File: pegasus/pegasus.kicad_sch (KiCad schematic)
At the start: 16 parts, among them IC1 L7805ACV, IC2 RFD900, IC3 L70B-M39, J1 Screw_Terminal_01x02, U1 Teensy4.0, U2 CON-SMA-EDGE-S, U3 CON-SMA-EDGE-S

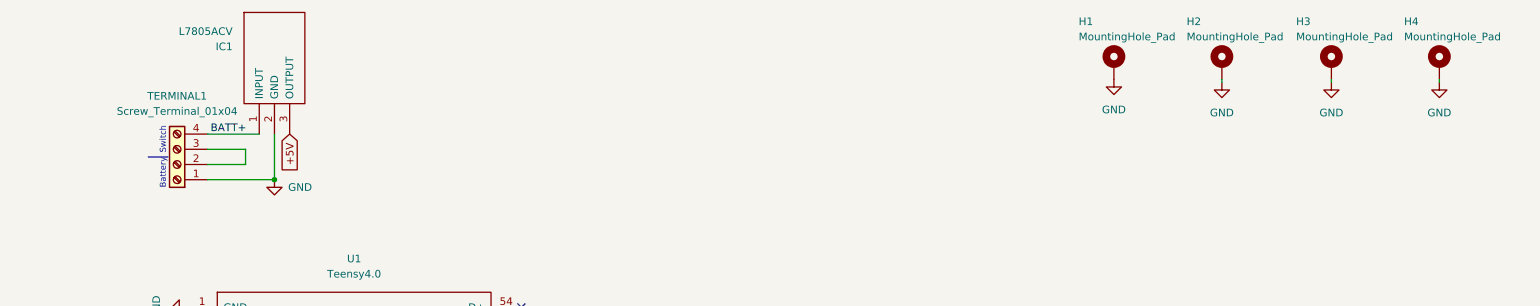
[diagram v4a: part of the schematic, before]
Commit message: change mount holes to m3, draft new component layout, reduce size  to 39x105mm
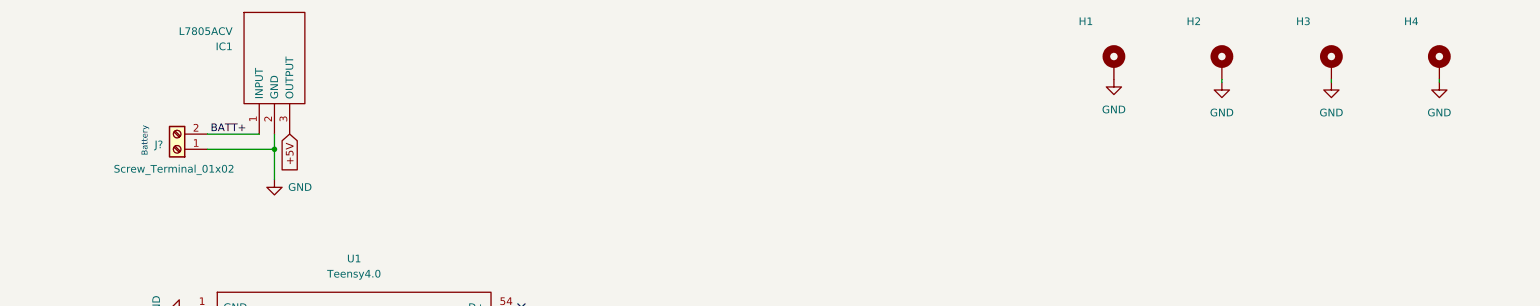
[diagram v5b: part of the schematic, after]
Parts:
- removed TERMINAL1: Screw_Terminal_01x04, RS-Components:SHDR4W100P0X500_1X4_2000X800X1000P, symbol Connector:Screw_Terminal_01x04
- added J?: Screw_Terminal_01x02, RS-Components:SHDR2W105P0X500_1X2_1060X900X1250P, symbol Connector:Screw_Terminal_01x02
- H1, H2, H3, H4: value MountingHole_Pad -> (none); footprint MountingHole:MountingHole_2.2mm_M2_Pad -> (none)
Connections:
- net BATT+: now also J?.2 (Pin_2)
- net GND: now also J?.1 (Pin_1)
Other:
- note removed: "Switch"
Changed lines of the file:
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@@
     (rev "1")
   )
-  (junction (at 56.134 42.164) (diameter 0) (color 0 0 0 0)
+  (junction (at 56.134 37.084) (diameter 0) (color 0 0 0 0)
   )
   (no_connect (at 97.3836 91.44))
@@
     (stroke (width 0) (type default) (color 0 0 0 0))
   )
-  (wire (pts (xy 56.134 34.544) (xy 56.134 42.164))
+  (wire (pts (xy 56.134 34.544) (xy 56.134 37.084))
     (stroke (width 0) (type default) (color 0 0 0 0))
   )
@@
     (stroke (width 0) (type default) (color 0 0 0 0))
   )
-  (wire (pts (xy 51.308 39.624) (xy 51.308 37.084))
-    (stroke (width 0) (type default) (color 0 0 0 0))
-  )
-  (wire (pts (xy 44.958 42.164) (xy 56.134 42.164))
-    (stroke (width 0) (type default) (color 0 0 0 0))
-  )
-  (wire (pts (xy 51.308 39.624) (xy 44.958 39.624))
+  (wire (pts (xy 44.958 37.084) (xy 56.134 37.084))
     (stroke (width 0) (type default) (color 0 0 0 0))
   )
@@
     (stroke (width 0) (type default) (color 0 0 0 0))
   )
-  (wire (pts (xy 51.308 37.084) (xy 44.958 37.084))
-    (stroke (width 0) (type default) (color 0 0 0 0))
-  )
-  (polyline (pts (xy 35.052 38.354) (xy 38.354 38.354))
-    (stroke (width 0) (type default) (color 0 0 0 0))
-  )
   (polyline (pts (xy 55.0164 197.9168) (xy 54.8132 154.6352))
     (stroke (width 0) (type default) (color 0 0 0 0))
   )
   (wire (pts (xy 117.6528 188.595) (xy 119.2784 188.595))
+    (stroke (width 0) (type default) (color 0 0 0 0))
+  )
+  (wire (pts (xy 56.134 37.084) (xy 56.134 42.164))
     (stroke (width 0) (type default) (color 0 0 0 0))
   )
@@
     (effects (font (size 1.27 1.27)) (justify left bottom))
   )
-  (text "Switch\n" (at 38.1 37.846 90)
-    (effects (font (size 1 1)) (justify left bottom))
-  )
   (text "RGB LED" (at 29.0068 154.7876 0)
     (effects (font (size 3 3)) (justify left bottom))
   )
-  (text "Battery" (at 38.1 38.608 270)
+  (text "Battery" (at 35.052 33.274 270)
     (effects (font (size 1 1)) (justify right bottom))
   )
@@
     (pin "1")
   )
+  (symbol (lib_id "Connector:Screw_Terminal_01x02") (at 39.878 37.084 180) (unit 1)
+    (in_bom yes) (on_board yes)
+    (property "Reference" "J?" (id 0) (at 36.83 36.322 0))
+    (property "Value" "Screw_Terminal_01x02" (id 1) (at 39.37 40.386 0))
+    (property "Footprint" "RS-Components:SHDR2W105P0X500_1X2_1060X900X1250P" (id 2) (at 39.878 37.084 0)
+      (effects (font (size 1.27 1.27)) hide)
+    )
+    (property "Datasheet" "~" (id 3) (at 39.878 37.084 0)
+      (effects (font (size 1.27 1.27)) hide)
+    )
+    (pin "1")
+    (pin "2")
+  )
   (symbol (lib_id "power:GND") (at 145.9484 179.07 90) (unit 1)
     (in_bom yes) (on_board yes) (fields_autoplaced)
@@
       (effects (font (size 1.27 1.27)) (justify left))
     )
-    (property "Value" "MountingHole_Pad" (id 1) (at 244.8052 18.288 0)
-      (effects (font (size 1.27 1.27)) (justify left))
-    )
-    (property "Footprint" "MountingHole:MountingHole_2.2mm_M2_Pad" (id 2) (at 250.698 22.86 0)
+    (property "Value" "" (id 1) (at 244.8052 18.288 0)
+      (effects (font (size 1.27 1.27)) (justify left))
+    )
+    (property "Footprint" "" (id 2) (at 250.698 22.86 0)
       (effects (font (size 1.27 1.27)) hide)
     )
@@
       (effects (font (size 1.27 1.27)) (justify left))
     )
-    (property "Value" "MountingHole_Pad" (id 1) (at 208.4832 18.288 0)
-      (effects (font (size 1.27 1.27)) (justify left))
-    )
-    (property "Footprint" "MountingHole:MountingHole_2.2mm_M2_Pad" (id 2) (at 214.376 22.86 0)
+    (property "Value" "" (id 1) (at 208.4832 18.288 0)
+      (effects (font (size 1.27 1.27)) (justify left))
+    )
+    (property "Footprint" "" (id 2) (at 214.376 22.86 0)
       (effects (font (size 1.27 1.27)) hide)
     )
@@
       (effects (font (size 1.27 1.27)) (justify left))
     )
-    (property "Value" "MountingHole_Pad" (id 1) (at 226.7712 18.288 0)
-      (effects (font (size 1.27 1.27)) (justify left))
-    )
-    (property "Footprint" "MountingHole:MountingHole_2.2mm_M2_Pad" (id 2) (at 232.664 22.86 0)
+    (property "Value" "" (id 1) (at 226.7712 18.288 0)
+      (effects (font (size 1.27 1.27)) (justify left))
+    )
+    (property "Footprint" "" (id 2) (at 232.664 22.86 0)
       (effects (font (size 1.27 1.27)) hide)
     )
@@
     )
     (pin "1")
-  )
-  (symbol (lib_id "Connector:Screw_Terminal_01x04") (at 39.878 39.624 180) (unit 1)
-    (in_bom no) (on_board yes) (fields_autoplaced)
-    (property "Reference" "TERMINAL1" (id 0) (at 39.878 28.194 0))
-    (property "Value" "Screw_Terminal_01x04" (id 1) (at 39.878 30.734 0))
-    (property "Footprint" "RS-Components:SHDR4W100P0X500_1X4_2000X800X1000P" (id 2) (at 39.878 39.624 0)
-      (effects (font (size 1.27 1.27)) hide)
-    )
-    (property "Datasheet" "~" (id 3) (at 39.878 39.624 0)
-      (effects (font (size 1.27 1.27)) hide)
-    )
-    (pin "1")
-    (pin "2")
-    (pin "3")
-    (pin "4")
   )
   (symbol (lib_id "Device:R_US") (at 42.7736 175.1584 180) (unit 1)
@@
       (effects (font (size 1.27 1.27)) (justify left))
     )
-    (property "Value" "MountingHole_Pad" (id 1) (at 190.4492 18.288 0)
-      (effects (font (size 1.27 1.27)) (justify left))
-    )
-    (property "Footprint" "MountingHole:MountingHole_2.2mm_M2_Pad" (id 2) (at 196.342 22.86 0)
+    (property "Value" "" (id 1) (at 190.4492 18.288 0)
+      (effects (font (size 1.27 1.27)) (justify left))
+    )
+    (property "Footprint" "" (id 2) (at 196.342 22.86 0)
       (effects (font (size 1.27 1.27)) hide)
     )
@@
     )
     (path "/fa097515-aa33-445e-a81c-63a2092f37d7"
-      (reference "H1") (unit 1) (value "MountingHole_Pad") (footprint "MountingHole:MountingHole_2.2mm_M2_Pad")
+      (reference "H1") (unit 1) (value "MountingHole_Pad") (footprint "MountingHole:MountingHole_3.2mm_M3_Pad")
     )
     (path "/9b4a3d5d-bec5-404f-9d07-6bbf9e73bbb6"
-      (reference "H2") (unit 1) (value "MountingHole_Pad") (footprint "MountingHole:MountingHole_2.2mm_M2_Pad")
+      (reference "H2") (unit 1) (value "MountingHole_Pad") (footprint "MountingHole:MountingHole_3.2mm_M3_Pad")
     )
     (path "/b9ff2bc9-2909-44de-b87f-01ae5ef3e5c6"
-      (reference "H3") (unit 1) (value "MountingHole_Pad") (footprint "MountingHole:MountingHole_2.2mm_M2_Pad")
+      (reference "H3") (unit 1) (value "MountingHole_Pad") (footprint "MountingHole:MountingHole_3.2mm_M3_Pad")
     )
     (path "/6d52c2cd-3d4d-4e9f-8991-6c4289d279ca"
-      (reference "H4") (unit 1) (value "MountingHole_Pad") (footprint "MountingHole:MountingHole_2.2mm_M2_Pad")
+      (reference "H4") (unit 1) (value "MountingHole_Pad") (footprint "MountingHole:MountingHole_3.2mm_M3_Pad")
     )
     (path "/57cb0745-7118-4f35-b7ad-15a440e8d2d7"
@@
       (reference "J1") (unit 1) (value "Screw_Terminal_01x02") (footprint "RS-Components:SHDR2W105P0X500_1X2_1060X900X1250P")
     )
+    (path "/4a35e1c8-7550-4a41-b483-1eb383f06ddc"
+      (reference "J?") (unit 1) (value "Screw_Terminal_01x02") (footprint "RS-Components:SHDR2W105P0X500_1X2_1060X900X1250P")
+    )
     (path "/40c73c82-ef5d-488c-b0d1-acd056d22f6f"
       (reference "R1") (unit 1) (value "220") (footprint "Resistor_SMD:R_1206_3216Metric_Pad1.30x1.75mm_HandSolder")
@@
       (reference "R3") (unit 1) (value "220") (footprint "Resistor_SMD:R_1206_3216Metric_Pad1.30x1.75mm_HandSolder")
     )
-    (path "/d4822f5d-8c1d-4b0c-ba23-0826fc0572d8"
-      (reference "TERMINAL1") (unit 1) (value "Screw_Terminal_01x04") (footprint "RS-Components:SHDR4W100P0X500_1X4_2000X800X1000P")
-    )
     (path "/1b9443a3-51ba-4b98-961a-84902a38a4f3"

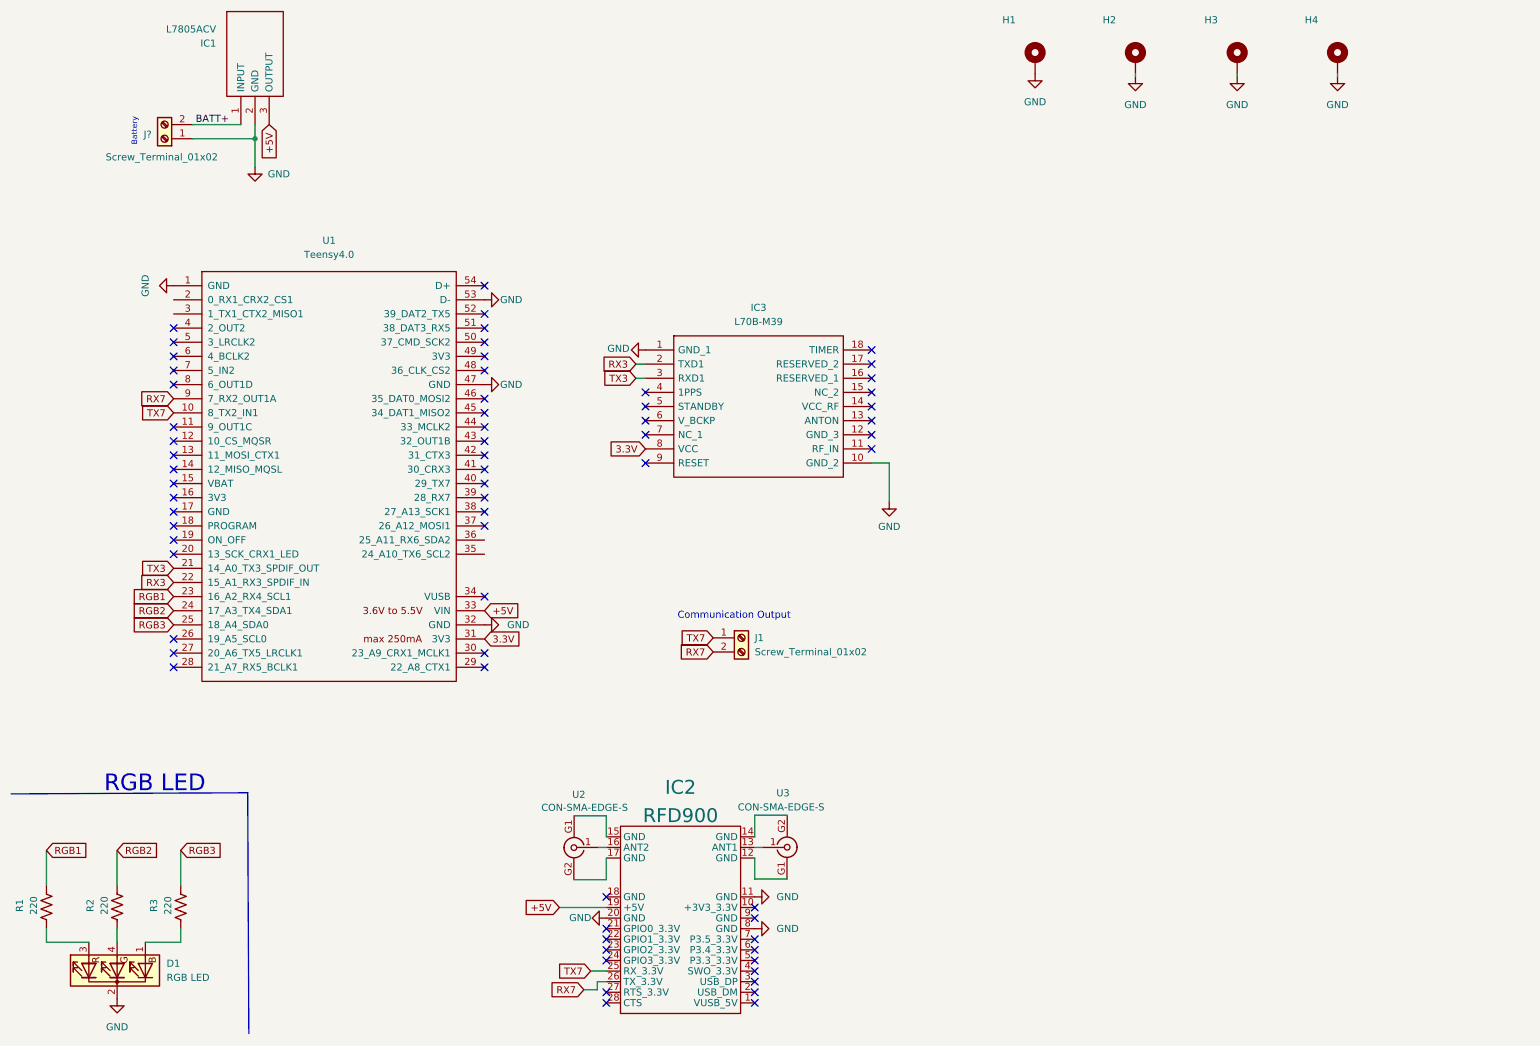
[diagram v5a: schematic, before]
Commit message: add second rx-tx screw terminal connector, optimize pin assignment for other components
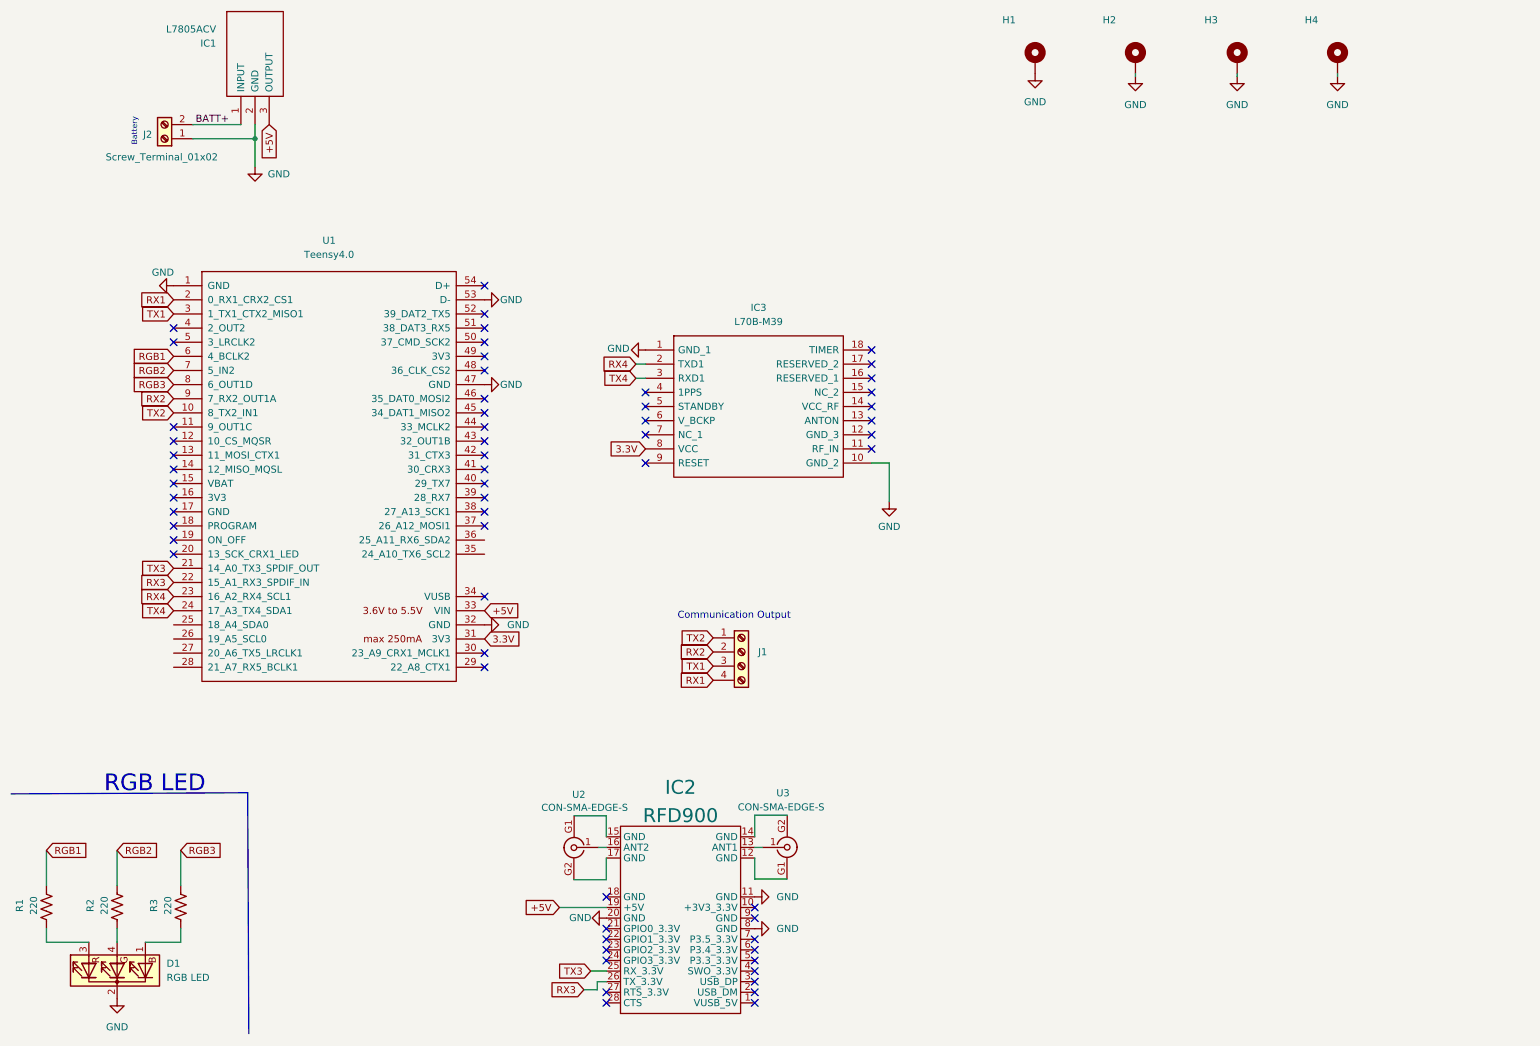
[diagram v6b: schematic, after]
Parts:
- removed J1: Screw_Terminal_01x02, RS-Components:SHDR2W105P0X500_1X2_1060X900X1250P, symbol Connector:Screw_Terminal_01x02
- added J1: (no value), symbol Connector:Screw_Terminal_01x04
- gave numbers to parts that had none: 1
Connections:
- net RGB1: now also U1.6 (4_BCLK2); no longer U1.23 (16_A2_RX4_SCL1)
- net RGB2: now also U1.7 (5_IN2); no longer U1.24 (17_A3_TX4_SDA1)
- net RGB3: now also U1.8 (6_OUT1D); no longer U1.25 (18_A4_SDA0)
- net RX3: now also IC2.26 (TX_3.3V); no longer IC3.2 (TXD1)
- net TX3: now also IC2.25 (RX_3.3V); no longer IC3.3 (RXD1)
- net RX1: now reaches U1.2 (0_RX1_CRX2_CS1)
- net RX1: now also J1.4 (Pin_4)
- net TX1: now reaches U1.3 (1_TX1_CTX2_MISO1)
- net TX1: now also J1.3 (Pin_3)
- net RX7 renamed RX2
- net RX2: now also J1.2 (Pin_2); no longer IC2.26 (TX_3.3V)
- net TX7 renamed TX2
- net TX2: now also J1.1 (Pin_1); no longer IC2.25 (RX_3.3V)
- new net RX4: IC3.2 (TXD1), U1.23 (16_A2_RX4_SCL1)
- new net TX4: IC3.3 (RXD1), U1.24 (17_A3_TX4_SDA1)
- no-connect marks 66 -> 60

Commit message: add xtsd footprint library, and xtsd nand chip to pcb
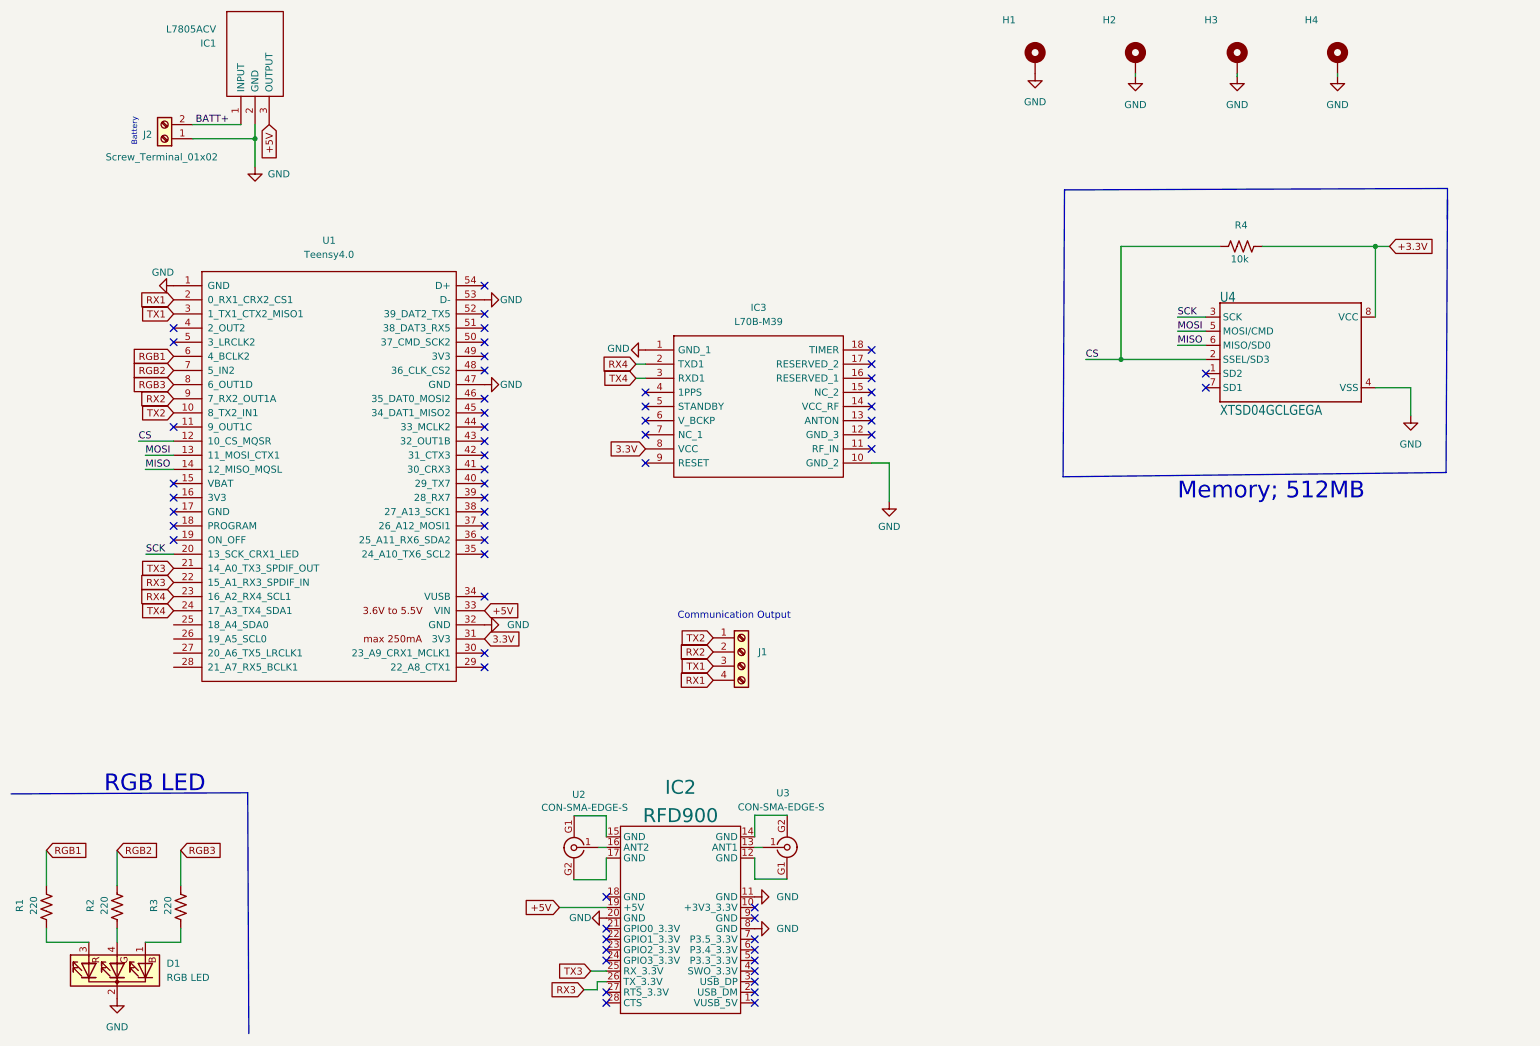
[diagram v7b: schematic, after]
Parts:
- added R4: 10k, Resistor_SMD:R_0805_2012Metric_Pad1.20x1.40mm_HandSolder, symbol Device:R_US
- added U4: XTSD04GCLGEGA, XTSD:LGA8_8X6, symbol Adafruit SPI Flash SD Card-eagle-import:SMT_SDCARD_8PIN
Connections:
- net GND: now also U4.4 (VSS)
- net CS: now reaches U1.12 (10_CS_MQSR)
- net CS: now also R4.2, U4.2 (SSEL/SD3)
- net MOSI: now reaches U1.13 (11_MOSI_CTX1)
- net MOSI: now also U4.5 (MOSI/CMD)
- net MISO: now reaches U1.14 (12_MISO_MQSL)
- net MISO: now also U4.6 (MISO/SD0)
- net SCK: now reaches U1.20 (13_SCK_CRX1_LED)
- net SCK: now also U4.3 (SCK)
- new net +3.3V: R4.1, U4.8 (VCC)
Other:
- note added: "Memory; 512MB"
